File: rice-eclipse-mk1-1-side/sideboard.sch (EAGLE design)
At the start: 56 parts, among them IC1 MCP6N11R, IC2 MCP6N11R, IC3 LMV321LICTRT, IC4 MCP6N11R, IC5 LMV321LICTRT, IC6 LMV321LICTRT, IC7 MCP6N11R, IC8 LMV321LICTRT

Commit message: New schematics for Titan amp
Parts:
- removed C2, C4, C6, C8: 10nF, rcl:C-USC0603
- removed C3, C5, C7: 1UF, rcl:C-USC0603
- removed CAA1, CAA2, CAA3, CAA4, CAA5, CAA6, CAA7, CAA8: (no value), rcl:C-US025-025X050
- removed CAL1, X4, X5, X7, X9: (no value), con-phoenix-254:MPT2
- removed IC4, IC7: MCP6N11R, microchip-extra:MCP6N11R
- removed IC5, IC6, IC8: LMV321LICTRT, st-microelectronics-extra:LMV321LICTRT
- removed RAA1, RAA2, RAA3, RAA4, RAA5, RAA6, RAA7, RAA8, RF2, RF3, RF4, RG3, RG4: (no value), rcl:R-US_0204/7
- removed RRN2, RRN3, RRN4, RRP2, RRP3, RRP4: (no value), rcl:R-US_R0805
- removed X11, X12, X13: (no value), con-phoenix-250-extra:1770924
- added JP1, JP2, JP3, JP4: (no value), pinhead:PINHD-1X2
- added RIN: 22k, rcl:R-US_0204/7
- added T1: 2N3904, transistor-neu-to92:2N3904
- added U6: 1101M2S3CQE2, SLIDE_SW:1101M2S3CQE2
- added X2: (no value), con-phoenix-250-extra:1770908
- IC2: value MCP6N11R -> XTR115; device microchip-extra:MCP6N11R -> texas-extra:XTR115
- X1: device con-phoenix-254:MPT2 -> con-phoenix-250-extra:1770908; SPICEPREFIX (none) -> X
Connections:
- removed net +3V3: C1.1, C2.1, C3.1, C4.1, C5.1, C6.1, C7.1, C8.1, CAL1-1.1, IC1.+V, IC2.+V, IC3.+VS, IC4.+V, IC5.+VS, IC6.+VS, IC7.+V, IC8.+VS, RRP2.2, RRP3.2, RRP4.2, RZ1.E, X4-2.1, X5-1.1, X7-1.1, X9-1.1
- removed net LC1_OUT: IC5.IN-, IC5.OUT, X11-1.SK
- removed net LC2_OUT: IC3.IN-, IC3.OUT, X11-2.SK
- removed net LC3_OUT: IC6.IN-, IC6.OUT, X11-3.SK
- removed net LC4_OUT1: IC8.IN-, IC8.OUT, X11-4.SK
- removed net N$12: IC1.+, X12-4.SK
- removed net N$13: IC2.ENCAL, X5-2.1
- removed net N$17: CAA3.1, RAA3.1, RAA4.2
- removed net N$19: IC2.REF, RG2.1, RRN2.2, RRP2.1
- removed net N$20: IC7.-, X13-1.SK
- removed net N$21: IC7.+, X13-2.SK
- removed net N$22: IC4.ENCAL, X7-2.1
- removed net N$23: IC4.OUT, RAA5.2, RF3.2
- removed net N$24: IC4.FG, RF3.1, RG3.2
- removed net N$26: CAA5.1, RAA5.1, RAA6.2
- removed net N$27: CAA6.1, IC6.IN+, RAA6.1
- removed net N$28: IC4.REF, RG3.1, RRN3.2, RRP3.1
- removed net N$29: IC4.+, X13-4.SK
- removed net N$30: IC4.-, X13-3.SK
- removed net N$31: IC7.ENCAL, X9-2.1
- removed net N$32: IC7.OUT, RAA7.2, RF4.2
- removed net N$33: IC7.FG, RF4.1, RG4.2
- removed net N$35: CAA7.1, RAA7.1, RAA8.2
- removed net N$36: CAA8.1, IC8.IN+, RAA8.1
- removed net N$37: IC7.REF, RG4.1, RRN4.2, RRP4.1
- new net +5V: C1.1, IC1.+V, IC3.+VS, JP1.1, JP4.2, RZ1.E, X1-1.SK
- new net IRET: C1.2, IC1.-V, IC3.-VS, JP2.1, RIN.1, RZ1.A, X1-4.SK
- new net N$10: IC1.+, X1-3.SK
- new net N$16: IC1.REF, JP3.2, U6.P
- new net V+: IC2.V+, T1.C, X2-1.SK
- net GND: now also IC2.GND, X2-2.SK; no longer C1.2, C2.2, C3.2, C4.2, C5.2, C6.2, C7.2, C8.2, CAA1.2, CAA2.2, CAA3.2, CAA4.2, CAA5.2, CAA6.2, CAA7.2, CAA8.2, IC1.-V, IC2.-V, IC3.-VS, IC4.-V, IC5.-VS, IC6.-VS, IC7.-V, IC8.-VS, RRN2.1, RRN3.1, RRN4.1, RZ1.A, X1-2.1
- net N$1: now also IC2.IRET, JP2.2; no longer IC2.+, X12-2.SK
- net N$11: now also X1-2.SK; no longer X12-3.SK
- net N$14: now also RG1.2, U6.S; no longer IC2.OUT, RAA3.2, RF2.2
- net N$15: now also IC3.IN+, RZ1.S; no longer IC2.FG, RF2.1, RG2.2
- net N$18: now also IC3.IN-, IC3.OUT, JP3.1; no longer CAA4.1, IC3.IN+, RAA4.1
- net N$2: now also IC2.I_IN, RIN.2; no longer IC2.-, X12-1.SK
- net N$3: now also IC2.VREG, JP4.1; no longer X1-1.1, X4-1.1
- net N$4: no longer RAA1.2
- net N$5: now also JP1.2; no longer CAL1-2.1
- net N$6: now also IC2.E, T1.E; no longer CAA1.1, RAA1.1, RAA2.2
- net N$7: now also RG1.1, RG2.1; no longer RG1.2
- net N$8: now also RG2.2, U6.O; no longer IC1.REF, RG1.1, RZ1.S
- net N$9: now also IC2.B, T1.B; no longer CAA2.1, IC5.IN+, RAA2.1
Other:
- moved on the sheet: IC3, RF1, RG1, RG2, RZ1

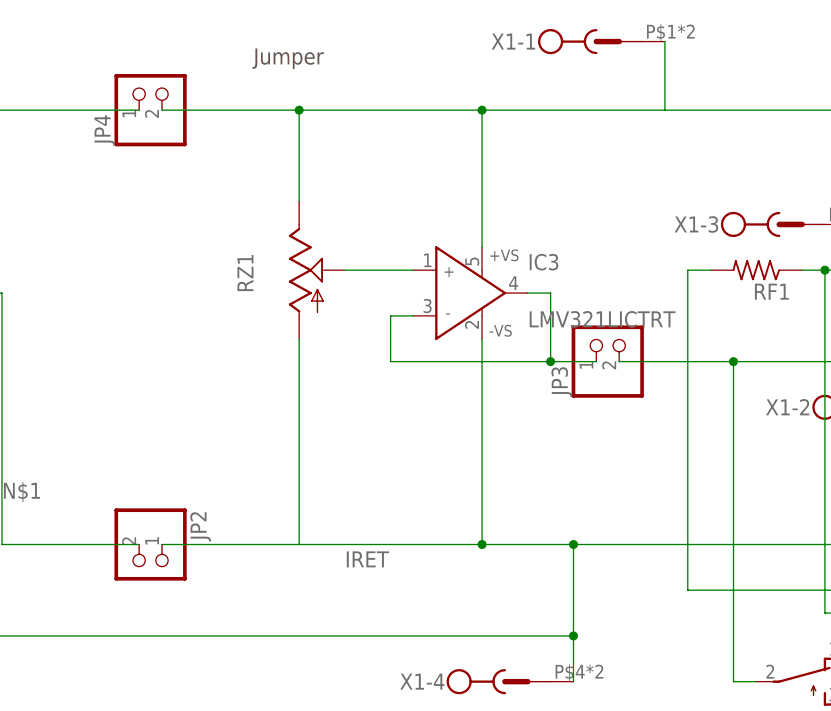
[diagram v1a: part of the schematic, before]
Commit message: Fixed some routing and minor mistakes with the underlying circuit.
TODO: still want to drill holes in the board.
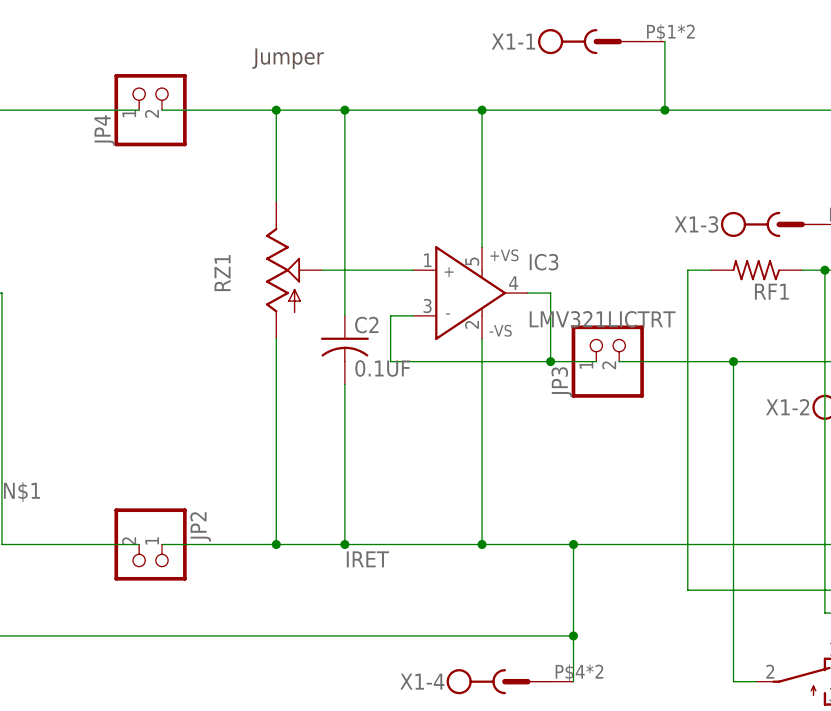
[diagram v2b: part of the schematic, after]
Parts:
- added C2: 0.1UF, rcl:C-USC0603
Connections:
- net +5V: now also C2.1
- net IRET: now also C2.2
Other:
- moved on the sheet: RZ1
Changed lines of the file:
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@@
 <part name="RG1" library="rcl" library_urn="urn:adsk.eagle:library:334" deviceset="R-US_" device="0204/7" package3d_urn="urn:adsk.eagle:package:23498/1"/>
 <part name="JP3" library="pinhead" library_urn="urn:adsk.eagle:library:325" deviceset="PINHD-1X2" device="" package3d_urn="urn:adsk.eagle:package:22435/2"/>
+<part name="C2" library="rcl" library_urn="urn:adsk.eagle:library:334" deviceset="C-US" device="C0603" package3d_urn="urn:adsk.eagle:package:23616/2" value="0.1UF"/>
 </parts>
 <sheets>
@@
 <instance part="RF1" gate="G$1" x="91.44" y="53.34" rot="R180"/>
 <instance part="C1" gate="G$1" x="134.62" y="55.88"/>
-<instance part="RZ1" gate="G$1" x="40.64" y="53.34"/>
+<instance part="RZ1" gate="G$1" x="38.1" y="53.34"/>
 <instance part="JP4" gate="G$1" x="25.4" y="73.66" rot="R90"/>
 <instance part="JP1" gate="G$1" x="121.92" y="63.5"/>
@@
 <instance part="RG1" gate="G$1" x="114.3" y="5.08" rot="R180"/>
 <instance part="JP3" gate="G$1" x="76.2" y="45.72" rot="R90"/>
+<instance part="C2" gate="G$1" x="45.72" y="45.72"/>
 </instances>
 <busses>
@@
 <wire x1="119.38" y1="71.12" x2="119.38" y2="66.04" width="0.1524" layer="91"/>
 <junction x="114.3" y="71.12"/>
-<wire x1="25.4" y1="71.12" x2="40.64" y2="71.12" width="0.1524" layer="91"/>
-<wire x1="40.64" y1="71.12" x2="60.96" y2="71.12" width="0.1524" layer="91"/>
+<wire x1="25.4" y1="71.12" x2="38.1" y2="71.12" width="0.1524" layer="91"/>
+<wire x1="38.1" y1="71.12" x2="45.72" y2="71.12" width="0.1524" layer="91"/>
 <pinref part="C1" gate="G$1" pin="1"/>
+<wire x1="45.72" y1="71.12" x2="60.96" y2="71.12" width="0.1524" layer="91"/>
 <wire x1="60.96" y1="71.12" x2="81.28" y2="71.12" width="0.1524" layer="91"/>
 <wire x1="81.28" y1="71.12" x2="114.3" y2="71.12" width="0.1524" layer="91"/>
@@
 <wire x1="134.62" y1="71.12" x2="119.38" y2="71.12" width="0.1524" layer="91"/>
 <junction x="119.38" y="71.12"/>
-<junction x="40.64" y="71.12"/>
+<junction x="38.1" y="71.12"/>
 <pinref part="RZ1" gate="G$1" pin="E"/>
-<wire x1="40.64" y1="60.96" x2="40.64" y2="71.12" width="0.1524" layer="91"/>
+<wire x1="38.1" y1="60.96" x2="38.1" y2="71.12" width="0.1524" layer="91"/>
 <pinref part="JP4" gate="G$1" pin="2"/>
 <pinref part="JP1" gate="G$1" pin="1"/>
@@
 <pinref part="X1" gate="-1" pin="SK"/>
 <wire x1="81.28" y1="78.74" x2="81.28" y2="71.12" width="0.1524" layer="91"/>
+<pinref part="C2" gate="G$1" pin="1"/>
+<wire x1="45.72" y1="48.26" x2="45.72" y2="71.12" width="0.1524" layer="91"/>
+<junction x="45.72" y="71.12"/>
+<junction x="81.28" y="71.12"/>
 </segment>
 </net>
@@
 <pinref part="C1" gate="G$1" pin="2"/>
 <wire x1="71.12" y1="22.86" x2="60.96" y2="22.86" width="0.1524" layer="91"/>
-<wire x1="60.96" y1="22.86" x2="40.64" y2="22.86" width="0.1524" layer="91"/>
+<wire x1="60.96" y1="22.86" x2="45.72" y2="22.86" width="0.1524" layer="91"/>
+<wire x1="45.72" y1="22.86" x2="38.1" y2="22.86" width="0.1524" layer="91"/>
 <wire x1="114.3" y1="33.02" x2="134.62" y2="33.02" width="0.1524" layer="91"/>
 <wire x1="134.62" y1="33.02" x2="134.62" y2="50.8" width="0.1524" layer="91"/>
 <junction x="114.3" y="33.02"/>
 <pinref part="RZ1" gate="G$1" pin="A"/>
-<wire x1="40.64" y1="45.72" x2="40.64" y2="22.86" width="0.1524" layer="91"/>
+<wire x1="38.1" y1="45.72" x2="38.1" y2="22.86" width="0.1524" layer="91"/>
 <pinref part="JP2" gate="G$1" pin="1"/>
-<wire x1="40.64" y1="22.86" x2="25.4" y2="22.86" width="0.1524" layer="91"/>
+<wire x1="38.1" y1="22.86" x2="25.4" y2="22.86" width="0.1524" layer="91"/>
 <label x="45.72" y="20.32" size="1.778" layer="95"/>
 <pinref part="X1" gate="-4" pin="SK"/>
@@
 <wire x1="2.54" y1="12.7" x2="71.12" y2="12.7" width="0.1524" layer="91"/>
 <junction x="71.12" y="12.7"/>
+<pinref part="C2" gate="G$1" pin="2"/>
+<wire x1="45.72" y1="40.64" x2="45.72" y2="22.86" width="0.1524" layer="91"/>
+<junction x="45.72" y="22.86"/>
+<junction x="38.1" y="22.86"/>
 </segment>
 </net>
@@
 <pinref part="IC3" gate="G$" pin="IN+"/>
 <pinref part="RZ1" gate="G$1" pin="S"/>
-<wire x1="45.72" y1="53.34" x2="53.34" y2="53.34" width="0.1524" layer="91"/>
+<wire x1="43.18" y1="53.34" x2="53.34" y2="53.34" width="0.1524" layer="91"/>
 </segment>
 </net>
@@
 </sheet>
 </sheets>
+<errors>
+</errors>
 </schematic>
 </drawing>
